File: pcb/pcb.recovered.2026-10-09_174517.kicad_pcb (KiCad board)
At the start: 2 copper layers, 305 x 104.8 mm, 155 parts, among them J1 AVR-ISP-6, SW1 ESCAPE, SW10 #9, SW11 #0, SW12 -_, SW13 =+, SW14 BKSPC, SW15 DELETE, SW16 TAB, SW17 Q, SW18 W, SW19 E, SW2 #1, SW20 R, SW21 T, SW22 Y, SW23 U, SW24 I, SW25 O, SW26 P, SW27 [{, SW28 ]}, SW29 \|, SW3 #2, SW30 `~, SW31 CAP, SW32 A, SW33 D, SW34 S, SW35 F, SW36 G, SW37 H, SW38 J, SW39 K, SW4 #3, SW40 L, SW41 ;:, SW42 '", SW43 ENTER, SW44 PGUP, SW45 SHIFT, SW46 Z, SW47 X, SW48 C, SW49 V, SW5 #4, SW50 B, SW51 N, SW52 M, SW53 ,<, SW54 .>, SW55 /?, SW56 SHIFT, SW57 UPROW, SW58 PGDOWN, SW59 CRTL, SW6 #5, SW60 WIN, SW61 ALT, SW62 SPACE, SW63 ALT, SW64 FN, SW65 LEFTROW, SW66 DOWNROW, SW67 RIGHTROW, SW7 #6, SW8 #7, SW9 #8, U1 PRTR5V0U2X, U2 ATmega32U4-A, Y1 Crystal_GND24_Small

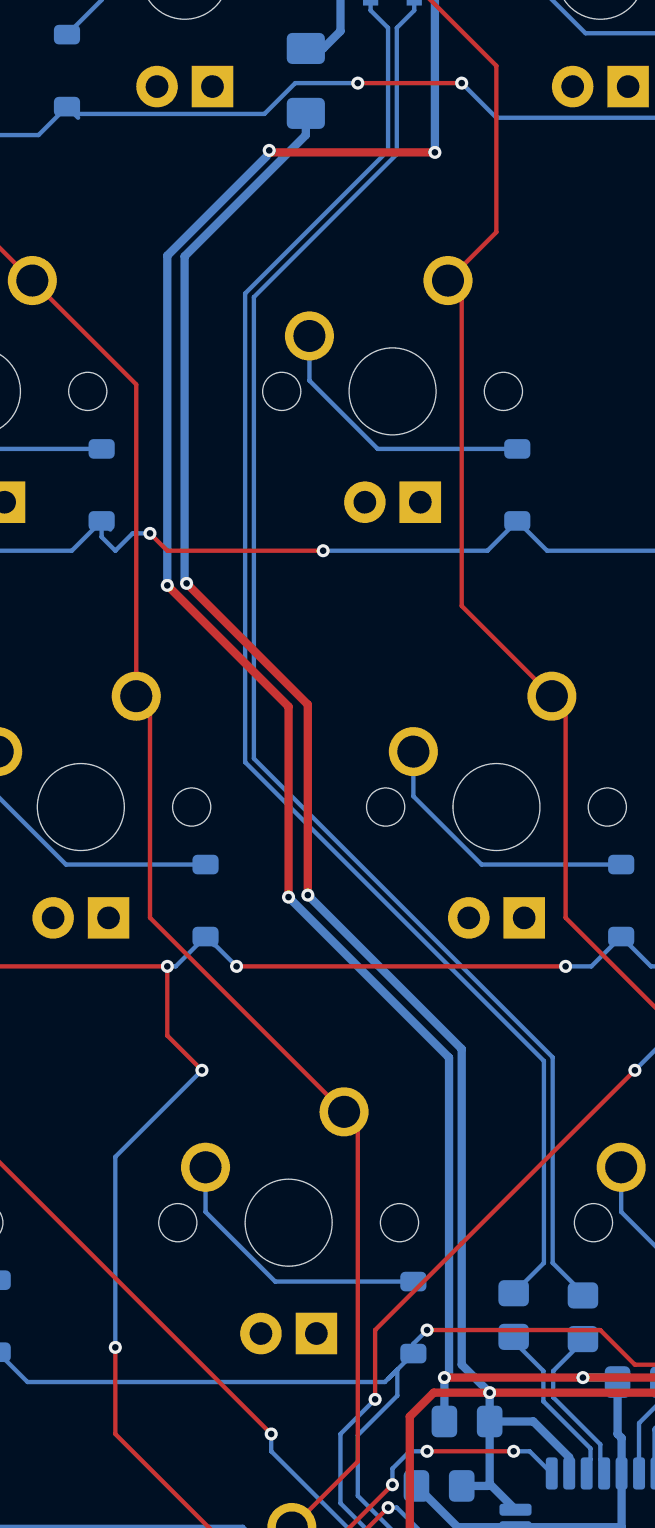
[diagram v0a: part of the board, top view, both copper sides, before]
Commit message: Changed to Kicad 10.07 and deleted old type C file
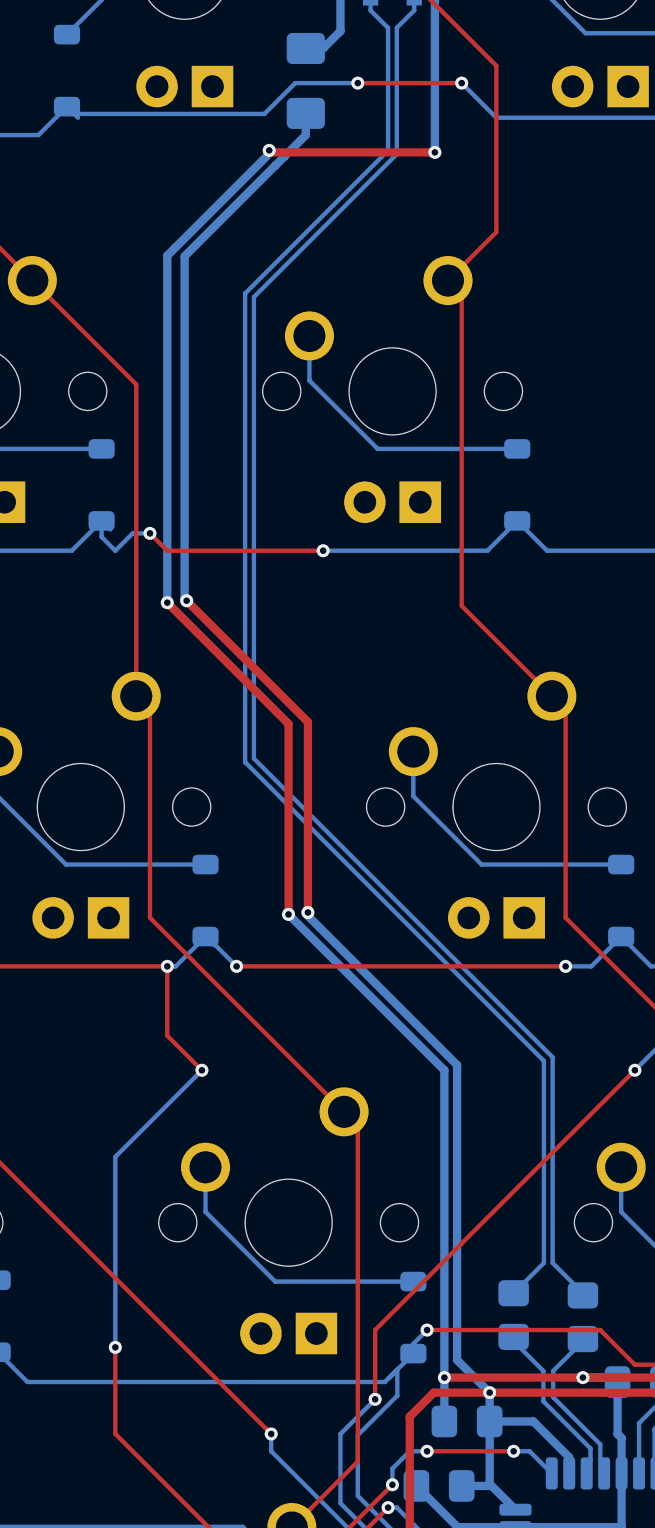
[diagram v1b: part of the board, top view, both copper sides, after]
